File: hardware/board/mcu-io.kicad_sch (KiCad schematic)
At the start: 29 parts

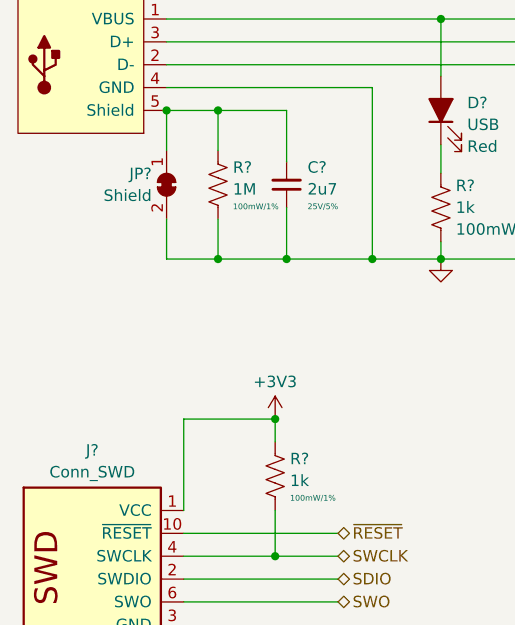
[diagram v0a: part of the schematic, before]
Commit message: Update resistor values in Vout DAC buffers
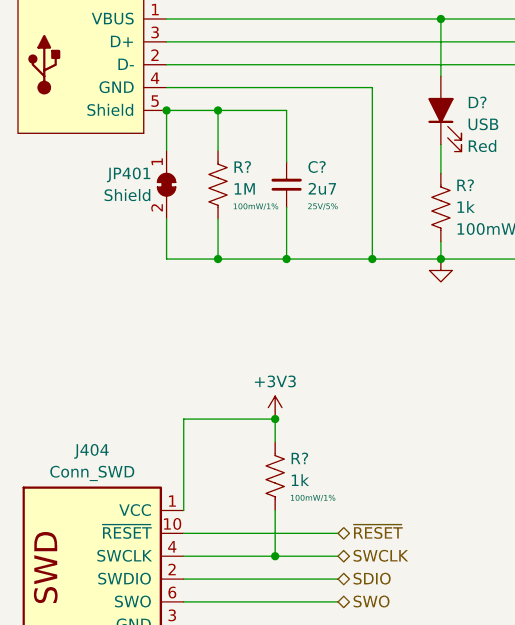
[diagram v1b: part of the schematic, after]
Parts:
- gave numbers to parts that had none: 2
